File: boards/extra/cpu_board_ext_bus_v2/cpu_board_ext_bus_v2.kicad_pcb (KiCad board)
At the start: 2 copper layers, 95.2 x 95.2 mm, 43 parts, among them J1 Exp. Conn. A, J2 Exp. Conn. B, J3 Power, J4 Exp. Conn. C, J5 EXT_CLK, J6 CPU_CLK_SEL, J7 BUS_CLK_SEL, U1 Z80CPPLC44, U2 GAL16V8, U3 74LS244, U4 74LS244, U5 74LS245, U6 74LS244, U7 74LS30, U8 ATF1502AS-7JX44, X1 INT_CLK

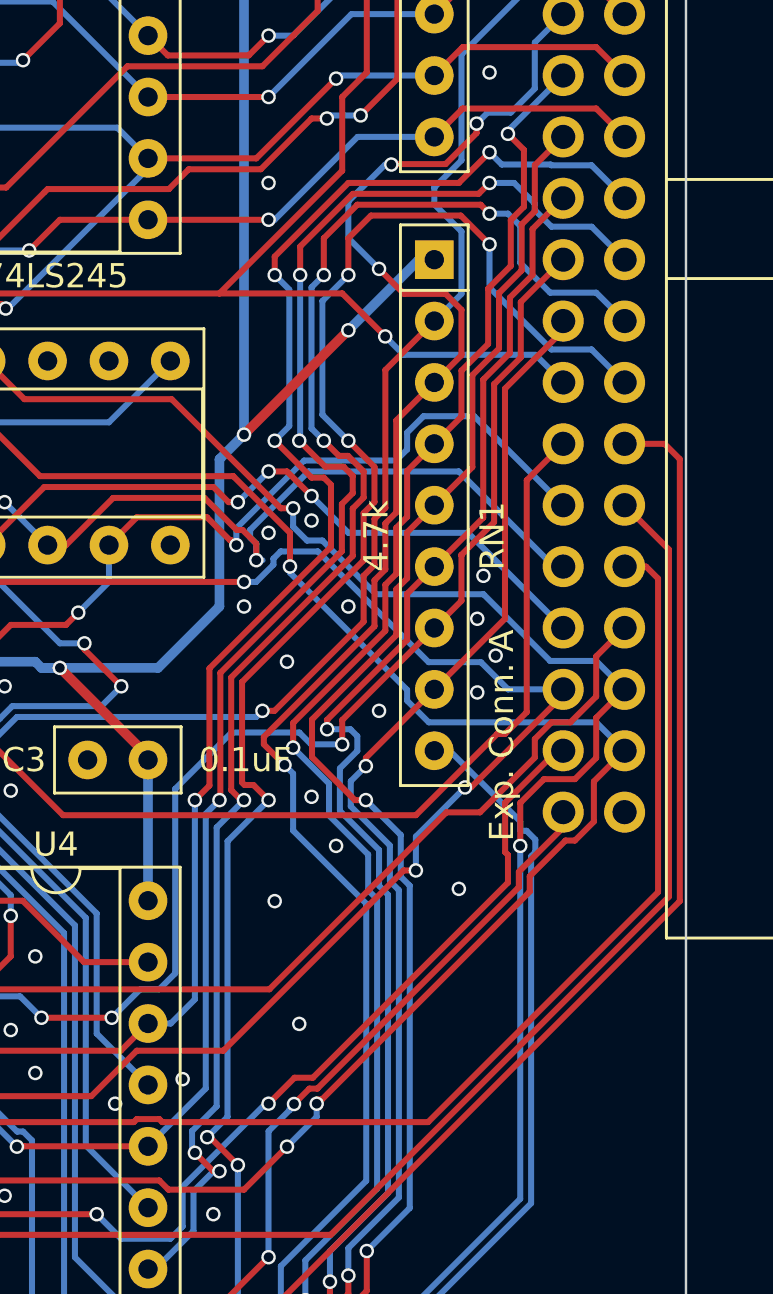
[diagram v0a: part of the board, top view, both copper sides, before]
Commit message: Removed CPU connection A14 and A15 from Expansion Bus Connector B.
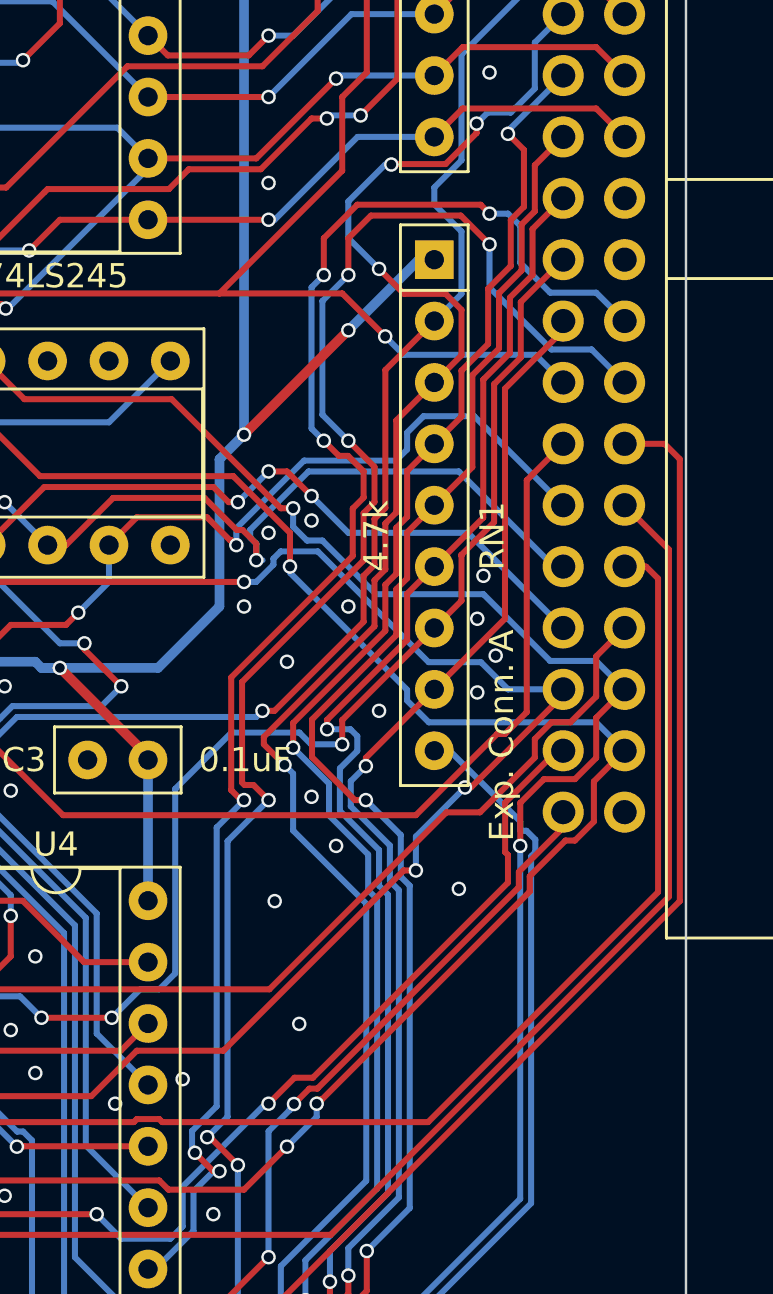
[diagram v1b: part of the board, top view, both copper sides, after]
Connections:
- J1 pad 20: /B_A15 -> unconnected-(J1-Pin_20-Pad20)
- J1 pad 22: /B_A14 -> unconnected-(J1-Pin_22-Pad22)
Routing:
- net /B_A14: track 130.4 -> 72.3 mm, vias 8 -> 4
- net /B_A15: track 134.0 -> 79.7 mm, vias 4 -> 0

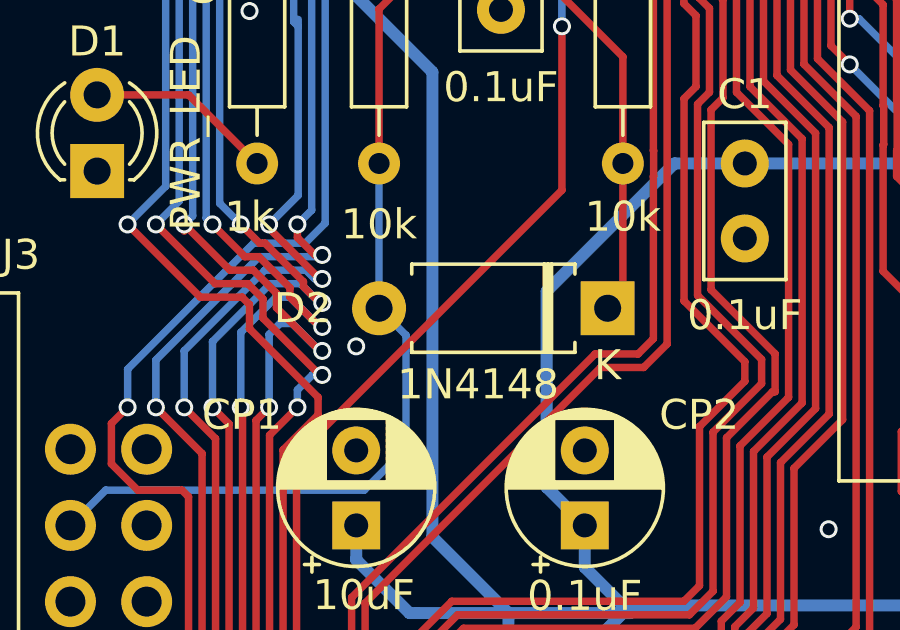
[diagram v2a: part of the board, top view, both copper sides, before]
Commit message: Changed footprint of D2 to DO-35.
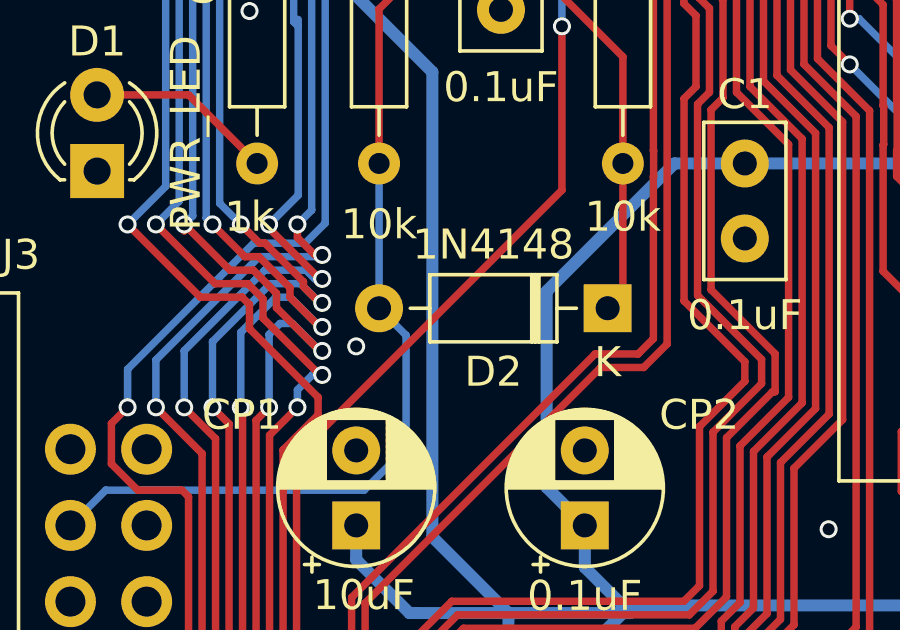
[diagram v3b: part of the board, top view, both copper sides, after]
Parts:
- D2: footprint Diode_THT:D_A-405_P7.62mm_Horizontal -> Diode_THT:D_DO-35_SOD27_P7.62mm_Horizontal

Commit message: Final commmit before upgrade to KiCad 8.0.x.
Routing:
- net /M_A17: track 191.5 -> 175.9 mm
- net /M_A14: track 197.5 -> 193.9 mm
- net /M_A18: track 171.1 -> 168.5 mm
- net /M_A15: track 185.8 -> 183.9 mm
- net /B_D6: track 159.7 -> 160.4 mm
- net /M_A21: track 149.5 -> 150.1 mm
- net /~{IOR}: track 121.7 -> 122.3 mm
- net /~{IOW}: track 125.3 -> 125.9 mm
- net /B_A14: track 72.3 -> 72.8 mm
- net /GND: vias 98 -> 104
